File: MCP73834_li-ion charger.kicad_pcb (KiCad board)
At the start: 2 copper layers, 40 x 15.7 mm, 17 parts, among them CON101 USB-MICRO-B, P102 CONN_01X06, P103 CONN_01X02, P104 CONN_01X02, U101 MCP73834-FCI/UN

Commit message: finished layout
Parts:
- U101: footprint Housings_SSOP:MSOP-10-1EP_3x3mm_Pitch0.5mm -> Housings_SSOP:MSOP-10_3x3mm_Pitch0.5mm
- moved D101 21.8 mm to (170.5, 105.8), turned to 0 degrees
- moved P103 1.07 mm to (199.1, 102.6)
- moved R104 0.05 mm to (181.3, 103.6)
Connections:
- net Net-(C101-Pad1) renamed /Vs
- net Net-(R105-Pad2) renamed /Th
- P102 pad 3: /Pg -> /Prog
- P102 pad 4: /Prog -> /Pg
- P103 pad 1: /Vb -> GND
- P103 pad 2: GND -> /Vb
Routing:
- net Net-(D101-Pad2): track 0.00 -> 25.5 mm
- net /Pg: track 0.00 -> 10.8 mm
- net /S1: track 0.00 -> 9.88 mm
- net Net-(R105-Pad1): track 0.00 -> 8.36 mm
- net /Vb: track 0.00 -> 8.15 mm, vias 0 -> 10
- net /S2: track 0.00 -> 8.02 mm
- net /Prog: track 0.00 -> 7.78 mm
- net /Vs: track 0.00 -> 3.11 mm, vias 0 -> 4
- net /Th: track 0.00 -> 2.80 mm
- net Net-(D103-Pad2): track 0.00 -> 2.39 mm
- net Net-(D102-Pad2): track 0.00 -> 2.39 mm
- net GND: track 0.00 -> 1.21 mm, vias 0 -> 35
- added copper zone on B.Cu, net /Vb
- added copper zone on F.Cu, net /Vb
- added copper zone on B.Cu, net /Vs
- added copper zone on F.Cu, net /Vs
- added copper zone on B.Cu, net GND
- added copper zone on F.Cu, net GND
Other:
- net class Default: clearance 0.254 -> 0.1524
- rule trace_clearance: 0.254 -> 0.1524

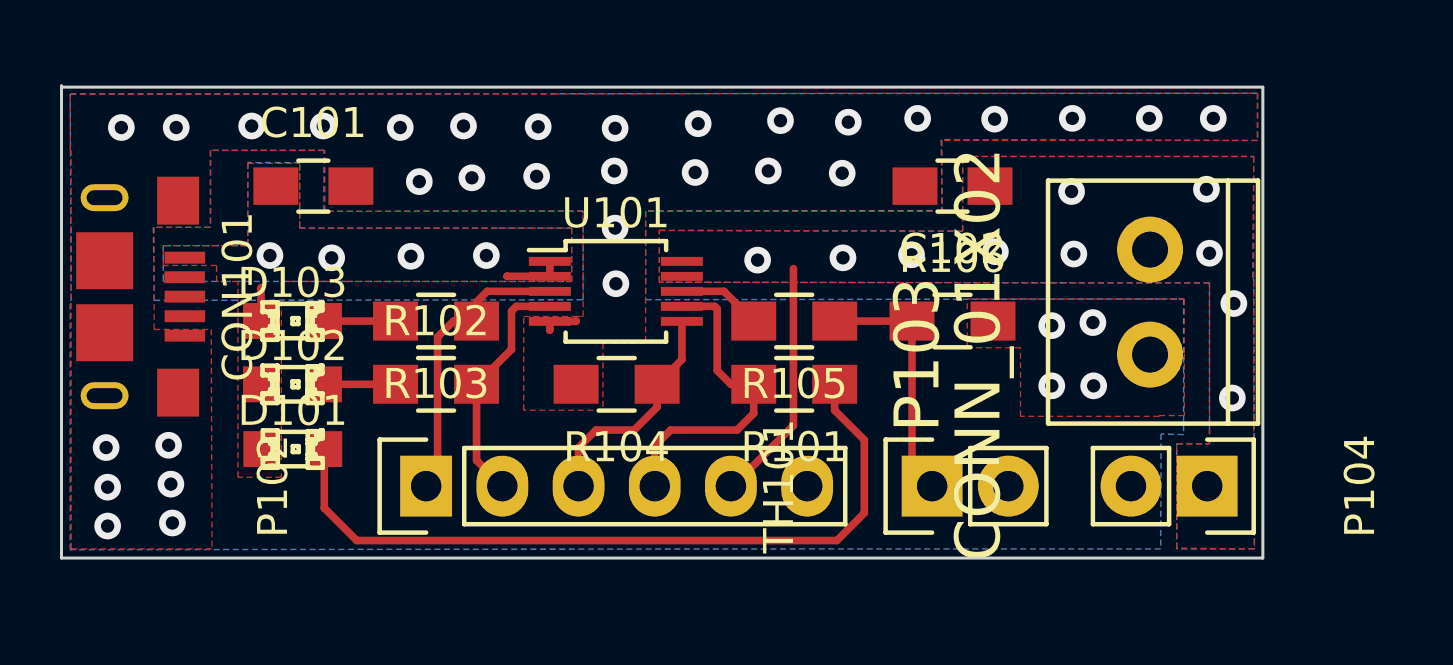
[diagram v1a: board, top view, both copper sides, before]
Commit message: changed layout
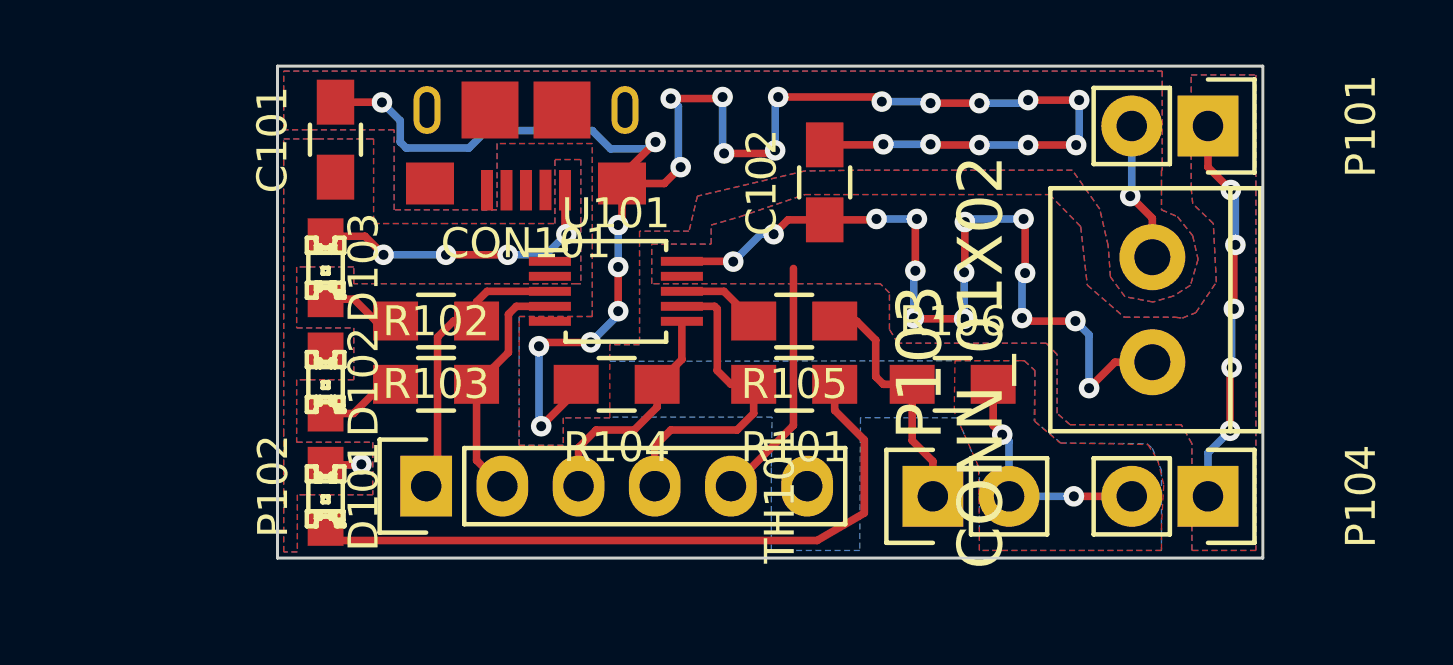
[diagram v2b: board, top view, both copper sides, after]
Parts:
- added P101: CONN_01X02, Pin_Headers:Pin_Header_Straight_1x02, F.Cu at (201.0, 95.0)
- moved CON101 15.4 mm to (178.3, 94.5), turned to 180 degrees
- moved C102 4.26 mm to (188.2, 96.9), turned to 90 degrees
- moved R106 2.11 mm to (192.5, 103.6)
- moved D103 2.09 mm to (171.6, 99.7), turned to 270 degrees
- moved D101 1.92 mm to (171.6, 107.3), turned to 270 degrees
- moved C101 1.71 mm to (171.9, 95.5), turned to 90 degrees
- moved D102 1.11 mm to (171.6, 103.5), turned to 270 degrees
- moved P104 0.34 mm to (201.0, 107.3)
- moved TH101 0.34 mm to (191.8, 107.3)
- moved P103 0.27 mm to (199.2, 102.9)
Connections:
- P103 pad 1: GND -> /Vb
- P103 pad 2: /Vb -> GND
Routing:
- net GND: track 1.21 -> 70.9 mm, vias 35 -> 27
- net /Vb: track 8.15 -> 50.0 mm, vias 10 -> 19
- net /Vs: track 3.11 -> 12.5 mm, vias 4 -> 5
- net Net-(D101-Pad2): track 25.5 -> 22.5 mm
- net Net-(D102-Pad2): track 2.39 -> 3.04 mm
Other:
- board size 40 x 15.7 mm -> 32.8 x 16.4 mm
- net class Default: via_dia 0.889 -> 0.6858; via_drill 0.635 -> 0.3302
- rule trace_min: 0.254 -> 0.1524
- rule via_min_drill: 0.508 -> 0.3302
- rule via_min_size: 0.889 -> 0.6858

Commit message: generated gerber files
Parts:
- removed P104: CONN_01X02, Pin_Headers:Pin_Header_Straight_1x02
- P101: footprint Pin_Headers:Pin_Header_Straight_1x02 -> B2B-PH-K-S
- moved R106 1.45 mm to (191.3, 102.8), turned to 270 degrees
- moved P103 1.32 mm to (199.1, 104.2)
- moved P101 1.21 mm to (200.6, 96.1)
- moved TH101 0.72 mm to (191.2, 107.0)
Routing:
- net GND: track 70.9 -> 61.6 mm, vias 27 -> 19
- net /Vb: track 50.0 -> 40.8 mm, vias 19 -> 13
- net /Vs: track 12.5 -> 14.8 mm, vias 5 -> 6
- net Net-(R105-Pad1): track 8.19 -> 9.16 mm
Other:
- board text added: "Li-Ion charger Rev 01 Bobrowicz"
